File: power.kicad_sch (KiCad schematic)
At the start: 10 parts

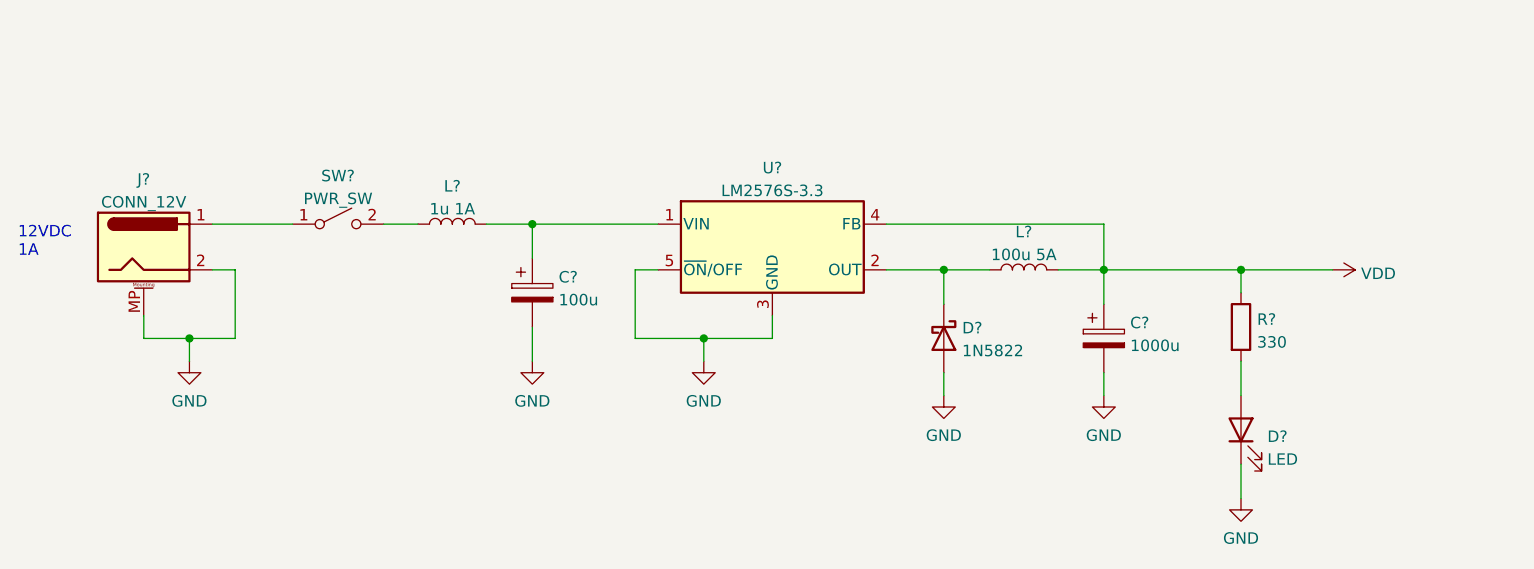
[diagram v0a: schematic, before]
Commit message: More capacitors for PSU
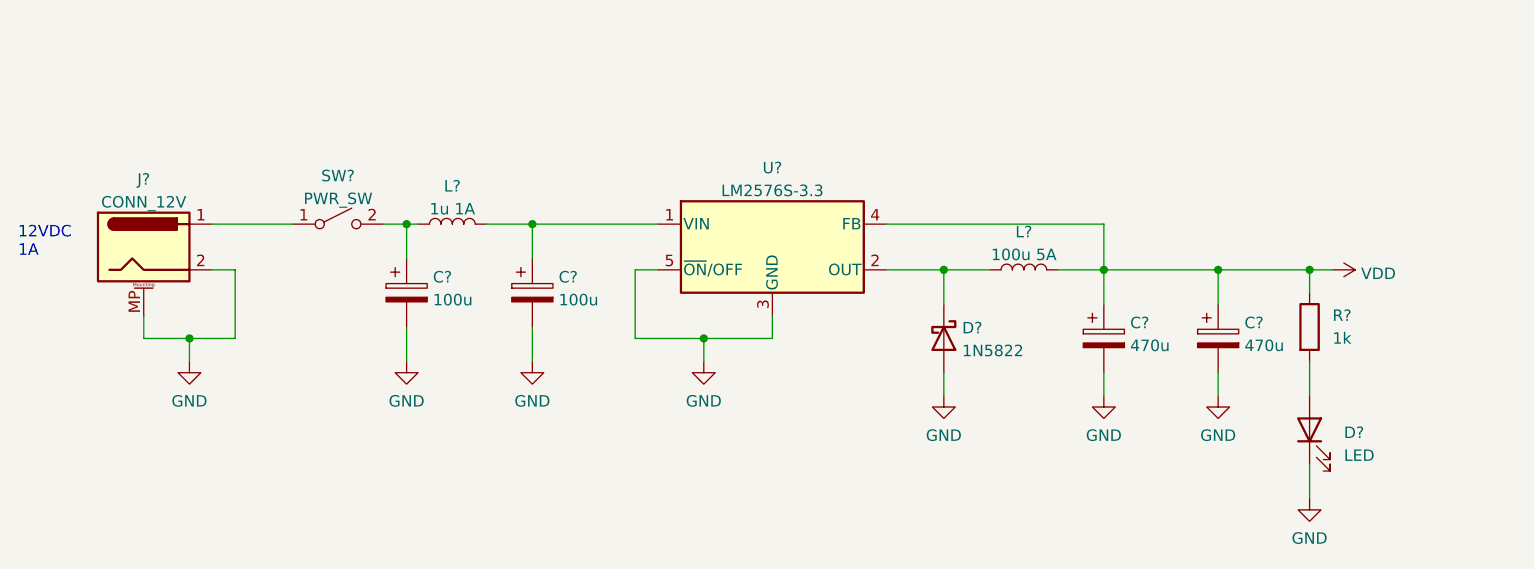
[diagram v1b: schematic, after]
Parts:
- added C?: 470u, symbol Device:C_Polarized
- added C?: 100u, symbol Device:C_Polarized
- C?: value 1000u -> 470u
- D?: footprint (none) -> LED_SMD:LED_PLCC-2_3.4x3.0mm_KA
- R?: value 330 -> 1k
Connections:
- net GND: now also C?.2, C?.2
- net VDD: now also C?.1
- net at L?.1, SW?.2 (B): now also C?.1
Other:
- moved on the sheet: D?, R?
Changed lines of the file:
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@@
 (kicad_sch (version 20211123) (generator eeschema)
   (paper "A4")
+  (junction (at 207.01 77.47) (diameter 0) (color 0 0 0 0)
+  )
   (junction (at 194.31 77.47) (diameter 0) (color 0 0 0 0)
   )
@@
   (junction (at 130.81 72.39) (diameter 0) (color 0 0 0 0)
   )
+  (junction (at 116.84 72.39) (diameter 0) (color 0 0 0 0)
+  )
   (junction (at 176.53 77.47) (diameter 0) (color 0 0 0 0)
   )
   (junction (at 92.71 85.09) (diameter 0) (color 0 0 0 0)
   )
-  (junction (at 209.55 77.47) (diameter 0) (color 0 0 0 0)
+  (junction (at 217.17 77.47) (diameter 0) (color 0 0 0 0)
   )
   (wire (pts (xy 142.24 85.09) (xy 149.86 85.09))
     (stroke (width 0) (type default) (color 0 0 0 0))
   )
+  (wire (pts (xy 207.01 77.47) (xy 217.17 77.47))
+    (stroke (width 0) (type default) (color 0 0 0 0))
+  )
   (wire (pts (xy 130.81 72.39) (xy 130.81 76.2))
     (stroke (width 0) (type default) (color 0 0 0 0))
@@
     (stroke (width 0) (type default) (color 0 0 0 0))
   )
-  (wire (pts (xy 209.55 87.63) (xy 209.55 91.44))
+  (wire (pts (xy 217.17 87.63) (xy 217.17 91.44))
     (stroke (width 0) (type default) (color 0 0 0 0))
   )
@@
     (stroke (width 0) (type default) (color 0 0 0 0))
   )
-  (wire (pts (xy 194.31 77.47) (xy 209.55 77.47))
-    (stroke (width 0) (type default) (color 0 0 0 0))
-  )
-  (wire (pts (xy 114.3 72.39) (xy 118.11 72.39))
+  (wire (pts (xy 116.84 72.39) (xy 116.84 76.2))
+    (stroke (width 0) (type default) (color 0 0 0 0))
+  )
+  (wire (pts (xy 194.31 77.47) (xy 207.01 77.47))
+    (stroke (width 0) (type default) (color 0 0 0 0))
+  )
+  (wire (pts (xy 114.3 72.39) (xy 116.84 72.39))
+    (stroke (width 0) (type default) (color 0 0 0 0))
+  )
+  (wire (pts (xy 207.01 77.47) (xy 207.01 81.28))
     (stroke (width 0) (type default) (color 0 0 0 0))
   )
@@
     (stroke (width 0) (type default) (color 0 0 0 0))
   )
-  (wire (pts (xy 209.55 99.06) (xy 209.55 102.87))
+  (wire (pts (xy 207.01 88.9) (xy 207.01 91.44))
+    (stroke (width 0) (type default) (color 0 0 0 0))
+  )
+  (wire (pts (xy 217.17 99.06) (xy 217.17 102.87))
     (stroke (width 0) (type default) (color 0 0 0 0))
   )
@@
     (stroke (width 0) (type default) (color 0 0 0 0))
   )
+  (wire (pts (xy 116.84 72.39) (xy 118.11 72.39))
+    (stroke (width 0) (type default) (color 0 0 0 0))
+  )
   (wire (pts (xy 170.18 72.39) (xy 194.31 72.39))
     (stroke (width 0) (type default) (color 0 0 0 0))
@@
     (stroke (width 0) (type default) (color 0 0 0 0))
   )
-  (wire (pts (xy 209.55 77.47) (xy 219.71 77.47))
+  (wire (pts (xy 217.17 77.47) (xy 219.71 77.47))
     (stroke (width 0) (type default) (color 0 0 0 0))
   )
@@
     (stroke (width 0) (type default) (color 0 0 0 0))
   )
-  (wire (pts (xy 209.55 77.47) (xy 209.55 80.01))
+  (wire (pts (xy 116.84 83.82) (xy 116.84 87.63))
+    (stroke (width 0) (type default) (color 0 0 0 0))
+  )
+  (wire (pts (xy 217.17 77.47) (xy 217.17 80.01))
     (stroke (width 0) (type default) (color 0 0 0 0))
   )
@@
     (pin "MP")
   )
-  (symbol (lib_id "power:GND") (at 209.55 102.87 0) (unit 1)
-    (in_bom yes) (on_board yes) (fields_autoplaced)
-    (property "Reference" "#PWR?" (id 0) (at 209.55 109.22 0)
-      (effects (font (size 1.27 1.27)) hide)
-    )
-    (property "Value" "GND" (id 1) (at 209.55 107.3134 0))
-    (property "Footprint" "" (id 2) (at 209.55 102.87 0)
-      (effects (font (size 1.27 1.27)) hide)
-    )
-    (property "Datasheet" "" (id 3) (at 209.55 102.87 0)
+  (symbol (lib_id "power:GND") (at 116.84 87.63 0) (unit 1)
+    (in_bom yes) (on_board yes) (fields_autoplaced)
+    (property "Reference" "#PWR?" (id 0) (at 116.84 93.98 0)
+      (effects (font (size 1.27 1.27)) hide)
+    )
+    (property "Value" "GND" (id 1) (at 116.84 92.0734 0))
+    (property "Footprint" "" (id 2) (at 116.84 87.63 0)
+      (effects (font (size 1.27 1.27)) hide)
+    )
+    (property "Datasheet" "" (id 3) (at 116.84 87.63 0)
+      (effects (font (size 1.27 1.27)) hide)
+    )
+    (pin "1")
+  )
+  (symbol (lib_id "power:GND") (at 217.17 102.87 0) (unit 1)
+    (in_bom yes) (on_board yes) (fields_autoplaced)
+    (property "Reference" "#PWR?" (id 0) (at 217.17 109.22 0)
+      (effects (font (size 1.27 1.27)) hide)
+    )
+    (property "Value" "GND" (id 1) (at 217.17 107.3134 0))
+    (property "Footprint" "" (id 2) (at 217.17 102.87 0)
+      (effects (font (size 1.27 1.27)) hide)
+    )
+    (property "Datasheet" "" (id 3) (at 217.17 102.87 0)
       (effects (font (size 1.27 1.27)) hide)
     )
@@
     (pin "5")
   )
-  (symbol (lib_id "Device:LED") (at 209.55 95.25 90) (unit 1)
-    (in_bom yes) (on_board yes) (fields_autoplaced)
-    (property "Reference" "D?" (id 0) (at 212.471 96.0028 90)
+  (symbol (lib_id "Device:LED") (at 217.17 95.25 90) (unit 1)
+    (in_bom yes) (on_board yes) (fields_autoplaced)
+    (property "Reference" "D?" (id 0) (at 220.98 95.5674 90)
       (effects (font (size 1.27 1.27)) (justify right))
     )
-    (property "Value" "LED" (id 1) (at 212.471 98.5397 90)
+    (property "Value" "LED" (id 1) (at 220.98 98.1074 90)
       (effects (font (size 1.27 1.27)) (justify right))
     )
-    (property "Footprint" "" (id 2) (at 209.55 95.25 0)
-      (effects (font (size 1.27 1.27)) hide)
-    )
-    (property "Datasheet" "~" (id 3) (at 209.55 95.25 0)
-      (effects (font (size 1.27 1.27)) hide)
-    )
-    (pin "1")
-    (pin "2")
-  )
-  (symbol (lib_id "Device:R") (at 209.55 83.82 0) (unit 1)
-    (in_bom yes) (on_board yes) (fields_autoplaced)
-    (property "Reference" "R?" (id 0) (at 211.328 82.9853 0)
-      (effects (font (size 1.27 1.27)) (justify left))
-    )
-    (property "Value" "330" (id 1) (at 211.328 85.5222 0)
-      (effects (font (size 1.27 1.27)) (justify left))
-    )
-    (property "Footprint" "" (id 2) (at 207.772 83.82 90)
-      (effects (font (size 1.27 1.27)) hide)
-    )
-    (property "Datasheet" "~" (id 3) (at 209.55 83.82 0)
-      (effects (font (size 1.27 1.27)) hide)
-    )
-    (pin "1")
-    (pin "2")
+    (property "Footprint" "LED_SMD:LED_PLCC-2_3.4x3.0mm_KA" (id 2) (at 217.17 95.25 0)
+      (effects (font (size 1.27 1.27)) hide)
+    )
+    (property "Datasheet" "~" (id 3) (at 217.17 95.25 0)
+      (effects (font (size 1.27 1.27)) hide)
+    )
+    (pin "1")
+    (pin "2")
+  )
+  (symbol (lib_id "Device:R") (at 217.17 83.82 0) (unit 1)
+    (in_bom yes) (on_board yes) (fields_autoplaced)
+    (property "Reference" "R?" (id 0) (at 219.71 82.5499 0)
+      (effects (font (size 1.27 1.27)) (justify left))
+    )
+    (property "Value" "1k" (id 1) (at 219.71 85.0899 0)
+      (effects (font (size 1.27 1.27)) (justify left))
+    )
+    (property "Footprint" "" (id 2) (at 215.392 83.82 90)
+      (effects (font (size 1.27 1.27)) hide)
+    )
+    (property "Datasheet" "~" (id 3) (at 217.17 83.82 0)
+      (effects (font (size 1.27 1.27)) hide)
+    )
+    (pin "1")
+    (pin "2")
+  )
+  (symbol (lib_id "Device:C_Polarized") (at 207.01 85.09 0) (unit 1)
+    (in_bom yes) (on_board yes) (fields_autoplaced)
+    (property "Reference" "C?" (id 0) (at 209.931 83.3663 0)
+      (effects (font (size 1.27 1.27)) (justify left))
+    )
+    (property "Value" "470u" (id 1) (at 209.931 85.9032 0)
+      (effects (font (size 1.27 1.27)) (justify left))
+    )
+    (property "Footprint" "" (id 2) (at 207.9752 88.9 0)
+      (effects (font (size 1.27 1.27)) hide)
+    )
+    (property "Datasheet" "~" (id 3) (at 207.01 85.09 0)
+      (effects (font (size 1.27 1.27)) hide)
+    )
+    (pin "1")
+    (pin "2")
+  )
+  (symbol (lib_id "Device:C_Polarized") (at 116.84 80.01 0) (unit 1)
+    (in_bom yes) (on_board yes) (fields_autoplaced)
+    (property "Reference" "C?" (id 0) (at 119.761 78.2863 0)
+      (effects (font (size 1.27 1.27)) (justify left))
+    )
+    (property "Value" "100u" (id 1) (at 119.761 80.8232 0)
+      (effects (font (size 1.27 1.27)) (justify left))
+    )
+    (property "Footprint" "" (id 2) (at 117.8052 83.82 0)
+      (effects (font (size 1.27 1.27)) hide)
+    )
+    (property "Datasheet" "~" (id 3) (at 116.84 80.01 0)
+      (effects (font (size 1.27 1.27)) hide)
+    )
+    (pin "1")
+    (pin "2")
+  )
+  (symbol (lib_id "power:GND") (at 207.01 91.44 0) (unit 1)
+    (in_bom yes) (on_board yes) (fields_autoplaced)
+    (property "Reference" "#PWR?" (id 0) (at 207.01 97.79 0)
+      (effects (font (size 1.27 1.27)) hide)
+    )
+    (property "Value" "GND" (id 1) (at 207.01 95.8834 0))
+    (property "Footprint" "" (id 2) (at 207.01 91.44 0)
+      (effects (font (size 1.27 1.27)) hide)
+    )
+    (property "Datasheet" "" (id 3) (at 207.01 91.44 0)
+      (effects (font (size 1.27 1.27)) hide)
+    )
+    (pin "1")
   )
   (symbol (lib_id "power:GND") (at 92.71 87.63 0) (unit 1)
@@
       (effects (font (size 1.27 1.27)) (justify left))
     )
-    (property "Value" "1000u" (id 1) (at 197.231 85.9032 0)
-      (effects (font (size 1.27 1.27)) (justify left))
-    )
+    (property "Value" "470u" (id 1) (at 197.231 85.9032 0)
+      (effects (font (size 1.27 1.27)) (justify left))
+    )

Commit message: Power supply design fine tuning
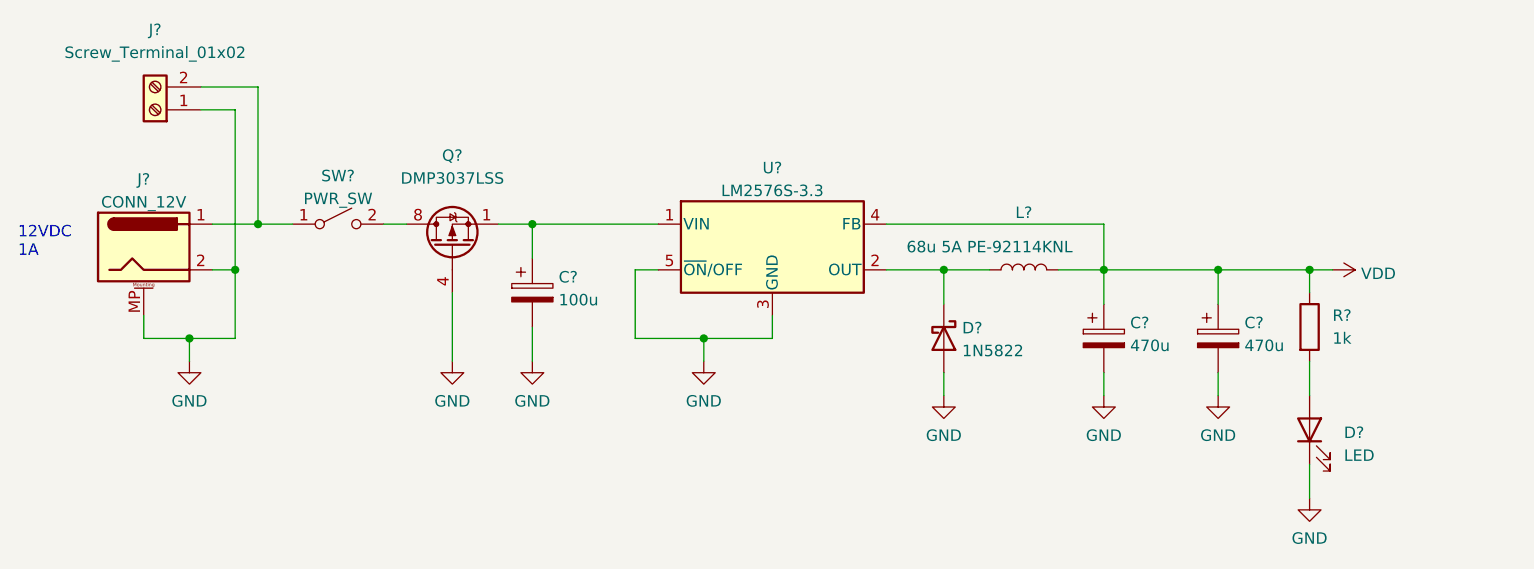
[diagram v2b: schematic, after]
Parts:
- removed C?: 100u, symbol Device:C_Polarized
- removed L?: 1u 1A, symbol Device:L
- added J?: Screw_Terminal_01x02, TerminalBlock_Phoenix:TerminalBlock_Phoenix_MKDS-1,5-2-5.08_1x02_P5.08mm_Horizontal, symbol Connector:Screw_Terminal_01x02
- added Q?: DMP3037LSS, Package_SO:SOIC-8_3.9x4.9mm_P1.27mm, symbol Transistor_FET:FDS9435A
- L?: value 100u 5A -> 68u 5A PE-92114KNL; footprint (none) -> Inductor_THT:L_Toroid_Vertical_L24.6mm_W15.5mm_P11.44mm_Pulse_KM-4
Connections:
- net GND: now also J?.1 (Pin_1), Q?.4 (G)
- net at J?.1, SW?.1 (A): now also J?.2 (Pin_2)
- net at C?.1, U?.1 (VIN): now also Q?.1 (S), Q?.2 (S), Q?.3 (S)
- net at SW?.2 (B): now also Q?.5 (D), Q?.6 (D), Q?.7 (D), Q?.8 (D)

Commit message: Capacitor part assignment
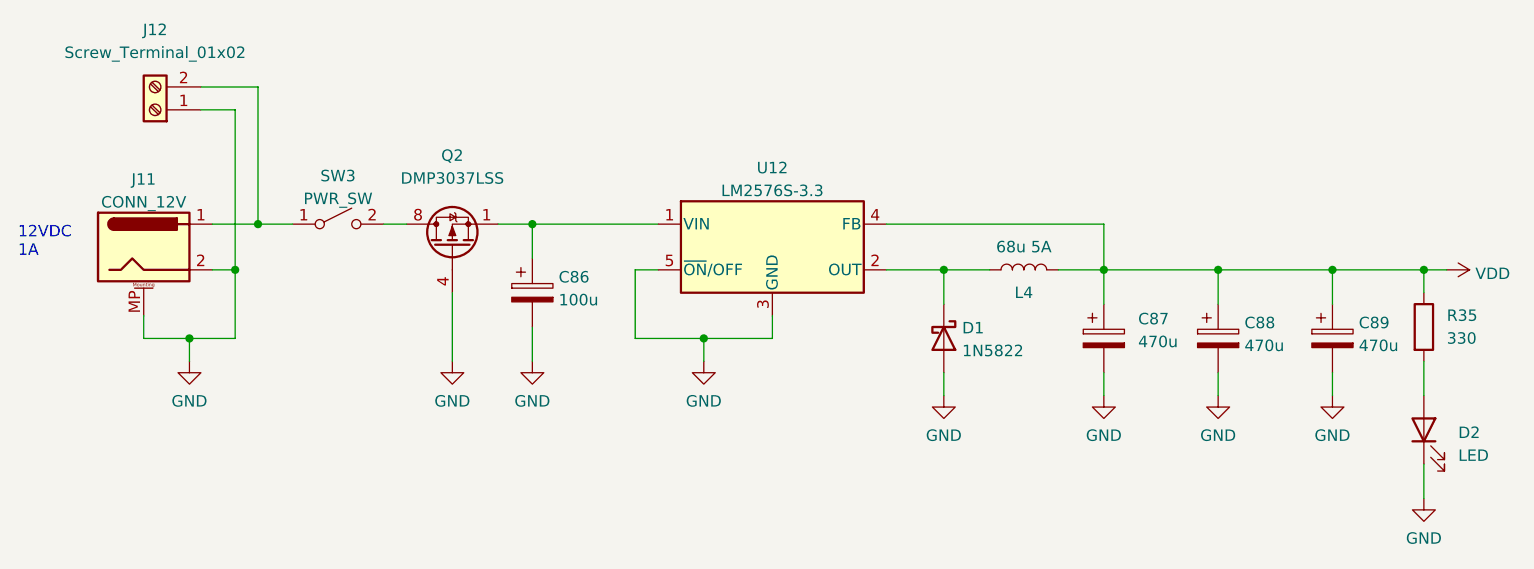
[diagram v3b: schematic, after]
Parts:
- added C89: 470u, Capacitor_THT:CP_Radial_D8.0mm_P5.00mm, symbol Device:C_Polarized
- C86: renamed from C?; footprint (none) -> Capacitor_THT:CP_Radial_D6.3mm_P2.50mm; Part (none) -> 710-860020473008
- C87, C88: renamed from C?; footprint (none) -> Capacitor_THT:CP_Radial_D8.0mm_P5.00mm; Part (none) -> 667-EEU-FR1C471B
- D1: renamed from D?; footprint (none) -> Diode_THT:D_DO-201AD_P5.08mm_Vertical_AnodeUp
- D2: renamed from D?; footprint LED_SMD:LED_PLCC-2_3.4x3.0mm_KA -> (none)
- L4: renamed from L?; value 68u 5A PE-92114KNL -> 68u 5A; Part (none) -> PE-92114KNL
- R35: renamed from R?; value 1k -> 330; footprint (none) -> Resistor_SMD:R_0603_1608Metric_Pad0.98x0.95mm_HandSolder
- gave numbers to parts that had none: 5
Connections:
- net GND: now also C89.2
- net VDD: now also C89.1
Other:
- moved on the sheet: D2, R35

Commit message: Add display connector
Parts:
- D2: footprint (none) -> LED_SMD:LED_PLCC-2_3.4x3.0mm_KA
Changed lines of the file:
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@@
       (effects (font (size 1.27 1.27)) (justify right))
     )
-    (property "Footprint" "" (id 2) (at 229.87 95.25 0)
+    (property "Footprint" "LED_SMD:LED_PLCC-2_3.4x3.0mm_KA" (id 2) (at 229.87 95.25 0)
       (effects (font (size 1.27 1.27)) hide)
     )

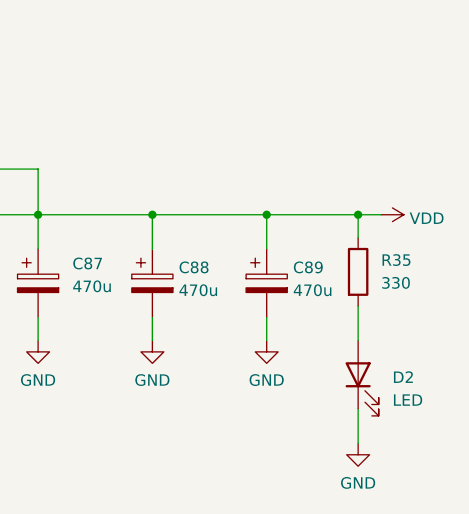
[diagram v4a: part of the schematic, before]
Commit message: Add extension connector, LEDs, buttons
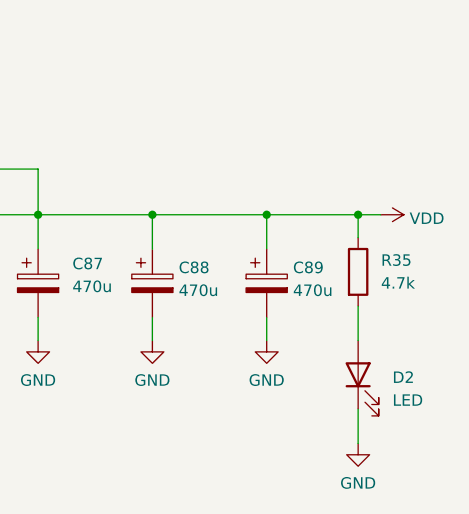
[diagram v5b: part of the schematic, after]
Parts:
- R35: value 330 -> 4.7k
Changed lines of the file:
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@@
       (effects (font (size 1.27 1.27)) (justify left))
     )
-    (property "Value" "330" (id 1) (at 232.41 85.0899 0)
+    (property "Value" "4.7k" (id 1) (at 232.41 85.0899 0)
       (effects (font (size 1.27 1.27)) (justify left))
     )
